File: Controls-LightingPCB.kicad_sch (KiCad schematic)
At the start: 10 parts, among them J1 PeripheralCANConnector, U1 PeripheralSOM

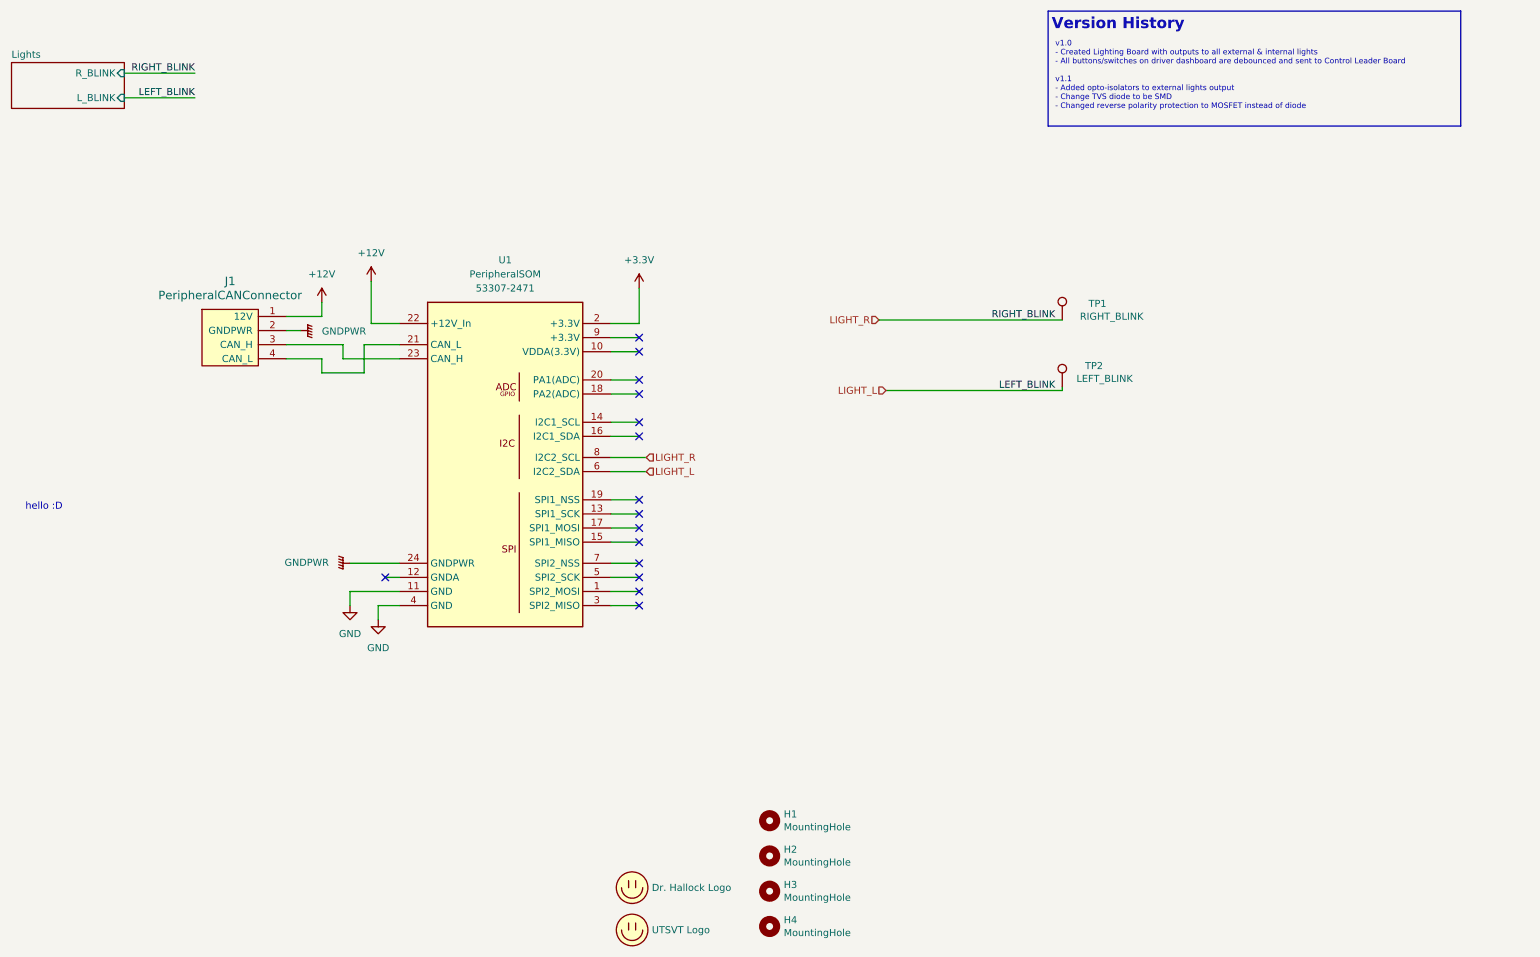
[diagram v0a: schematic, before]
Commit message: accommodated for 6 lights on one board, added test points and leds on board
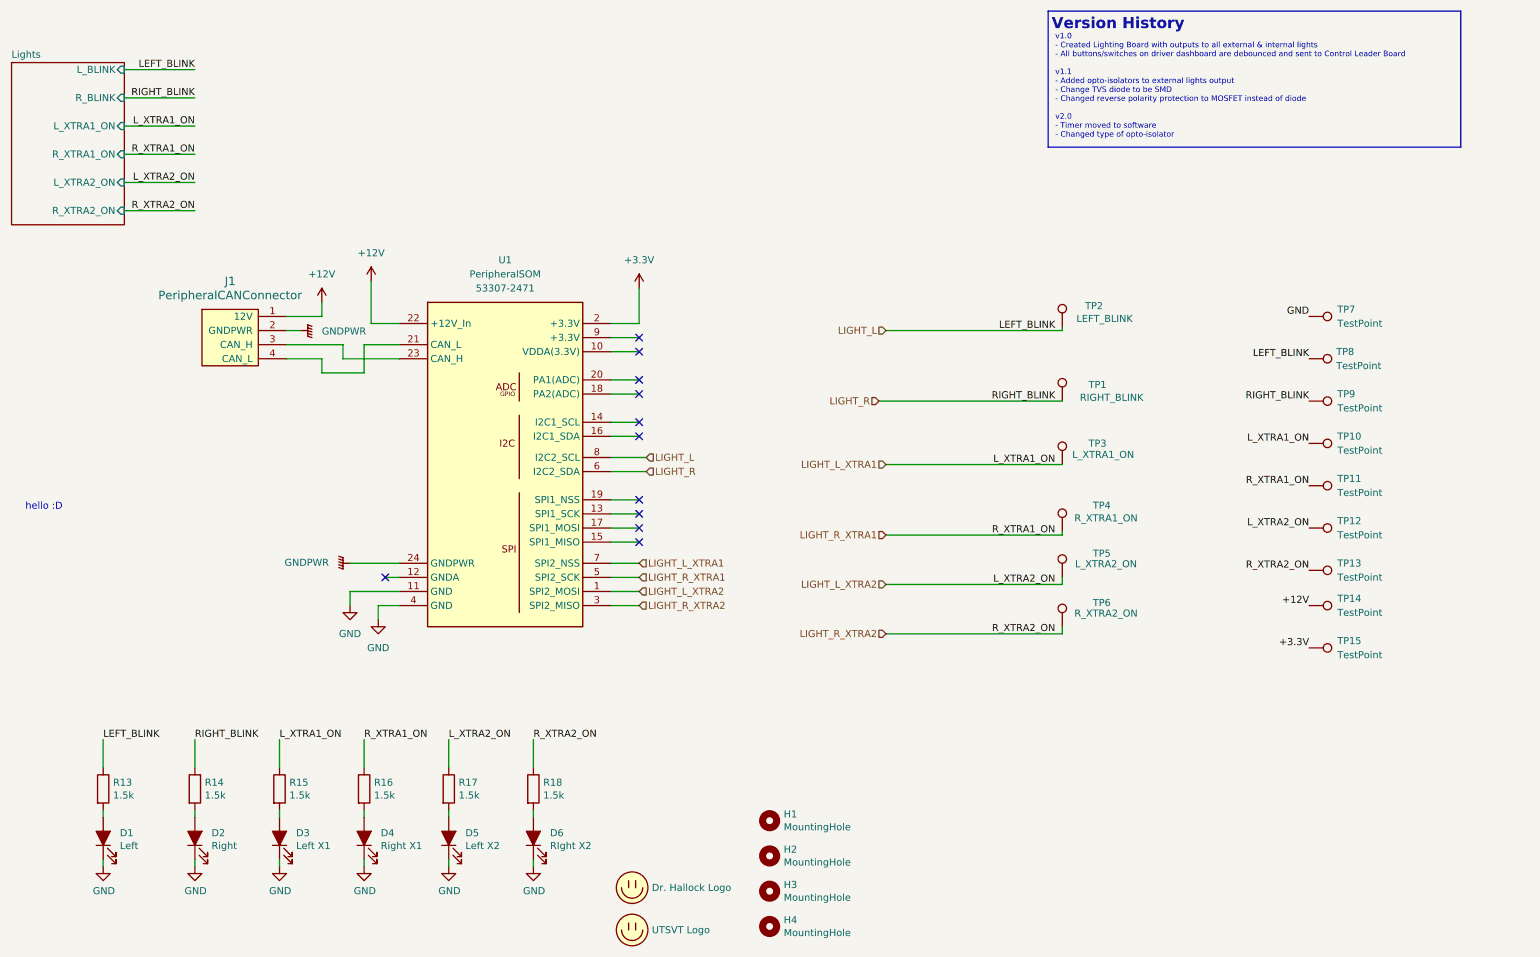
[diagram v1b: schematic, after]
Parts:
- added D1: Left, LED_SMD:LED_0805_2012Metric, symbol Device:LED_ALT
- added D2: Right, LED_SMD:LED_0805_2012Metric, symbol Device:LED_ALT
- added D3: Left X1, LED_SMD:LED_0805_2012Metric, symbol Device:LED_ALT
- added D4: Right X1, LED_SMD:LED_0805_2012Metric, symbol Device:LED_ALT
- added D5: Left X2, LED_SMD:LED_0805_2012Metric, symbol Device:LED_ALT
- added D6: RIght X2, LED_SMD:LED_0805_2012Metric, symbol Device:LED_ALT
- added R13, R14, R15, R16, R17, R18: 1.5k, Resistor_SMD:R_0805_2012Metric, symbol Device:R
- added TP10, TP11, TP12, TP13, TP14, TP15, TP7, TP8, TP9: TestPoint, symbol Connector:TestPoint
- added TP3: L_XTRA1_ON, TestPoint:TestPoint_Pad_1.5x1.5mm, symbol Connector:TestPoint
- added TP4: R_XTRA1_ON, TestPoint:TestPoint_Pad_1.5x1.5mm, symbol Connector:TestPoint
- added TP5: L_XTRA2_ON, TestPoint:TestPoint_Pad_1.5x1.5mm, symbol Connector:TestPoint
- added TP6: R_XTRA2_ON, TestPoint:TestPoint_Pad_1.5x1.5mm, symbol Connector:TestPoint
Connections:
- net +12V: now also TP14.1
- net +3.3V: now also TP15.1
- net GND: now also D1.1 (K), D2.1 (K), D3.1 (K), D4.1 (K), D5.1 (K), D6.1 (K), TP7.1
- net LIGHT_L: now also U1.8 (I2C2_SCL), R13.1, TP8.1; no longer U1.6 (I2C2_SDA)
- net LIGHT_R: now also U1.6 (I2C2_SDA), R14.1, TP9.1; no longer U1.8 (I2C2_SCL)
- net LIGHT_L_XTRA2: now reaches U1.1 (SPI2_MOSI)
- net LIGHT_L_XTRA2: now also R17.1, TP12.1, TP5.1
- net LIGHT_R_XTRA2: now reaches U1.3 (SPI2_MISO)
- net LIGHT_R_XTRA2: now also R18.1, TP13.1, TP6.1
- net LIGHT_R_XTRA1: now reaches U1.5 (SPI2_SCK)
- net LIGHT_R_XTRA1: now also R16.1, TP11.1, TP4.1
- net LIGHT_L_XTRA1: now reaches U1.7 (SPI2_NSS)
- net LIGHT_L_XTRA1: now also R15.1, TP10.1, TP3.1
- new net: D6.2 (A), R18.2
- new net: D2.2 (A), R14.2
- new net: D5.2 (A), R17.2
- new net: D4.2 (A), R16.2
- new net: D1.2 (A), R13.2
- new net: D3.2 (A), R15.2
- no-connect marks 15 -> 11
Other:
- sheet Lights ports: added L_XTRA1_ON, L_XTRA2_ON, R_XTRA1_ON, R_XTRA2_ON; removed none
- note added: "v1.0 - Created Lighting Board with outputs to all external & internal lights - All buttons/switches on driver dashboard are debounced and sent to Control Leader Board v1.1 - Added opto-isolators to external lights output - Change TVS diode to be SMD - Changed reverse polarity protection to MOSFET instead of diode v2.0 - Timer moved to software - Changed type of opto-isolator"
- note removed: "v1.0 - Created Lighting Board with outputs to all external & internal lights - All buttons/switches on driver dashboard are debounced and sent to Control Leader Board v1.1 - Added opto-isolators to external lights output - Change TVS diode to be SMD - Changed reverse polarity protection to MOSFET instead of diode"
- moved on the sheet: TP1, TP2

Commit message: simplified circuit and reduced testpoints
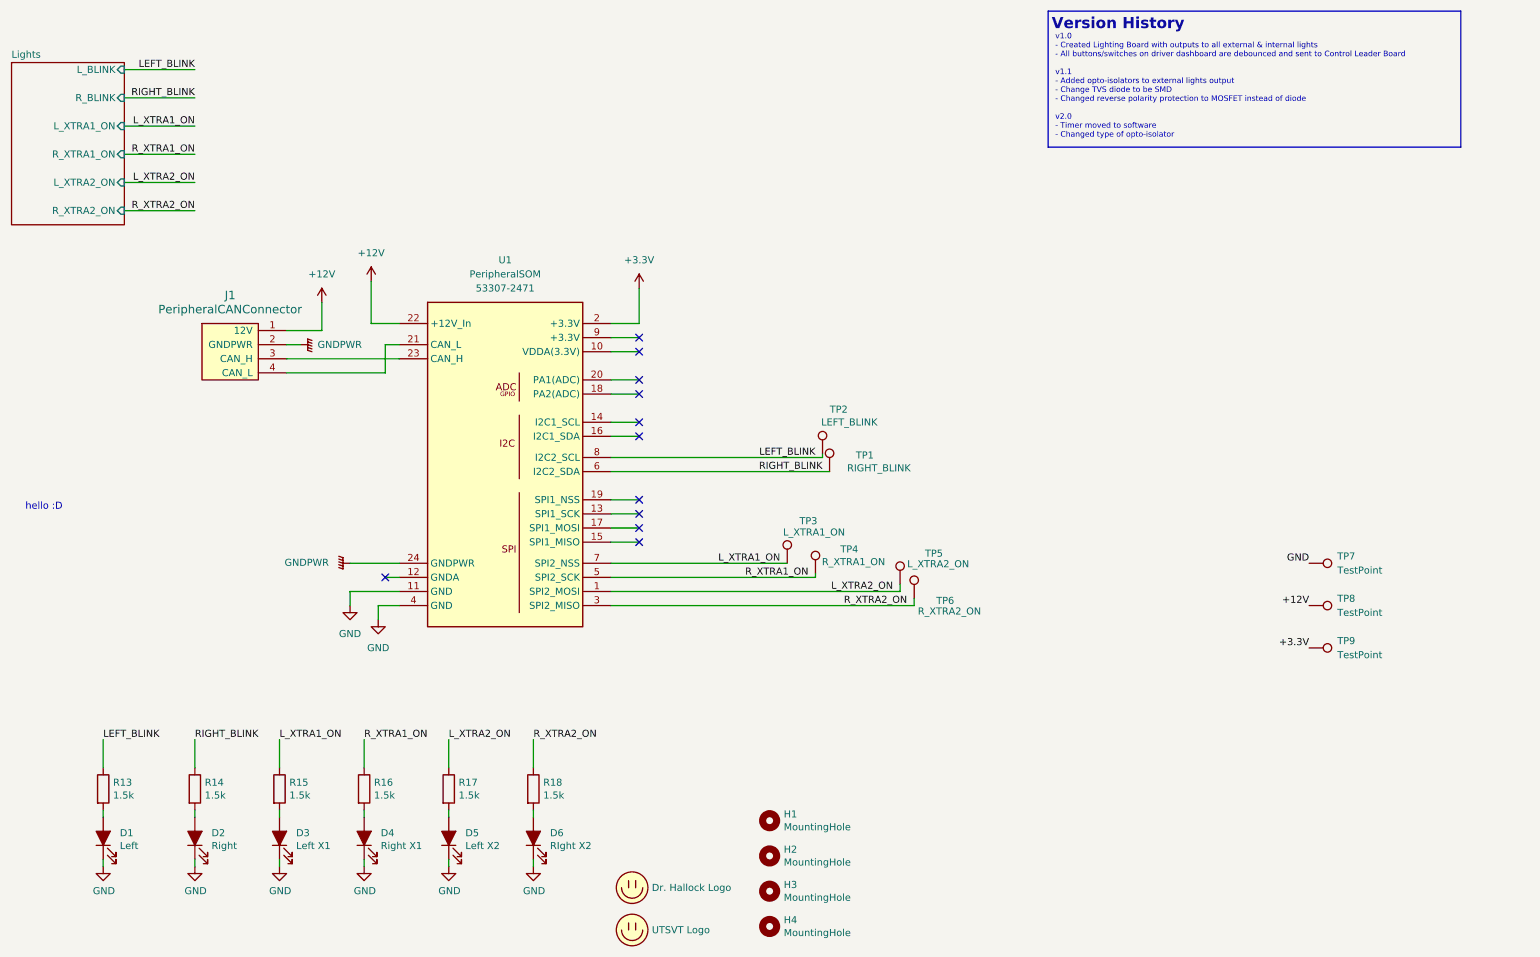
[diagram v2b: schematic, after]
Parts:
- removed TP10, TP11, TP12, TP13, TP8, TP9: TestPoint, symbol Connector:TestPoint
- renumbered TP14 to TP8, TP15 to TP9
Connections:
- net LIGHT_L renamed LEFT_BLINK
- net LIGHT_L_XTRA1 renamed L_XTRA1_ON
- net LIGHT_L_XTRA2 renamed L_XTRA2_ON
- net LIGHT_R renamed RIGHT_BLINK
- net LIGHT_R_XTRA1 renamed R_XTRA1_ON
- net LIGHT_R_XTRA2 renamed R_XTRA2_ON
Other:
- moved on the sheet: J1, TP1, TP2, TP3, TP4, TP5, TP6, TP7

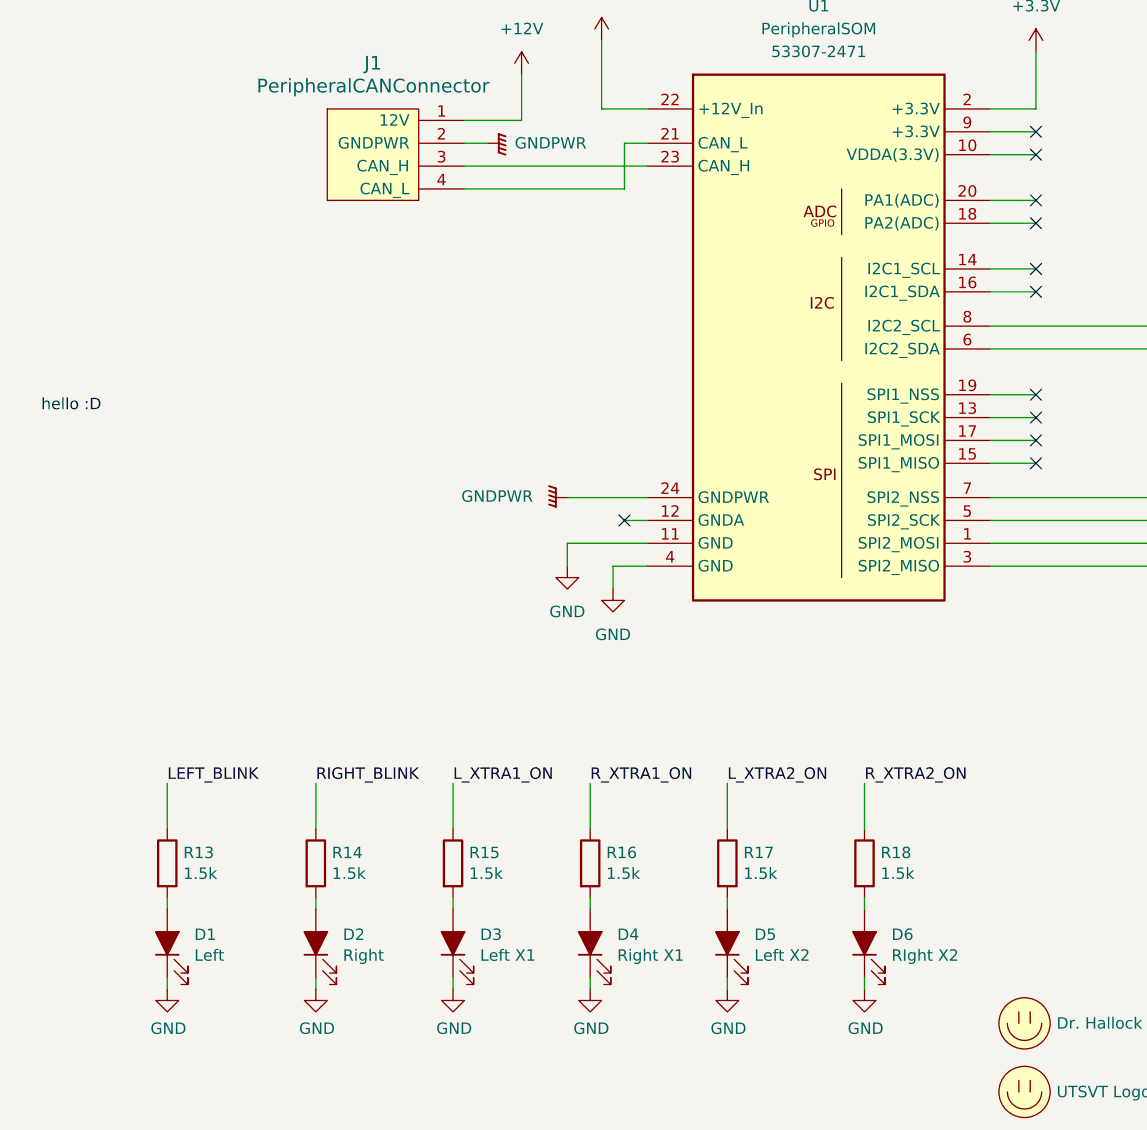
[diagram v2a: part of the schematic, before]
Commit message: added second can connector and changed resistor values for SMD LEDs
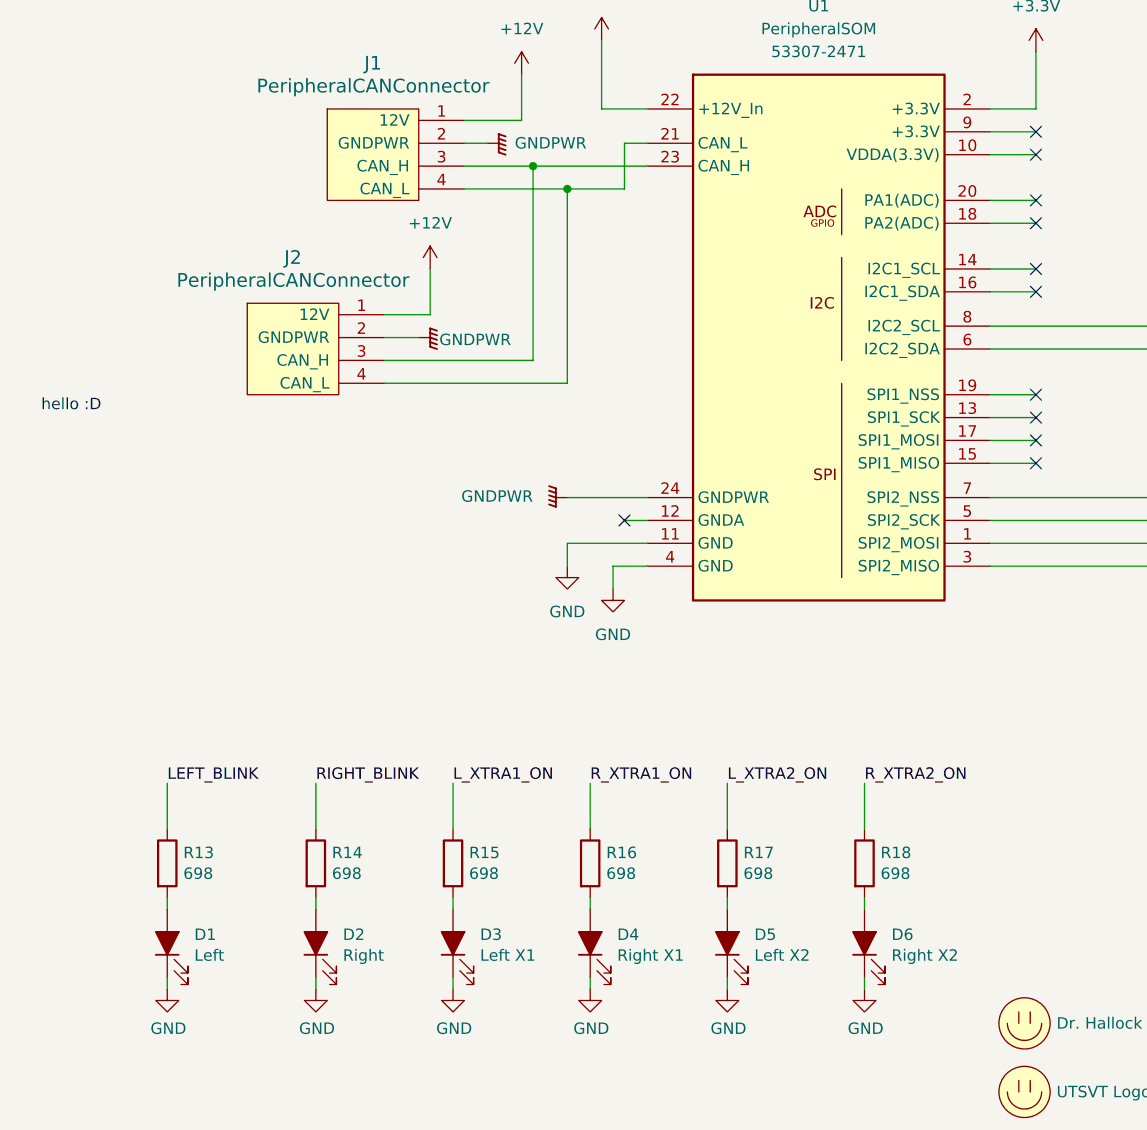
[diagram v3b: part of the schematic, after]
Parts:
- added J2: PeripheralCANConnector, UTSVT_Connectors:Molex_MicroFit3.0_1x4xP3.00mm_PolarizingPeg_Vertical, symbol utsvt-connectors:PeripheralCANConnector
- D6: value RIght X2 -> Right X2
- R13, R14, R15, R16, R17, R18: value 1.5k -> 698
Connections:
- net +12V: now also J2.1 (12V)
- net GNDPWR: now also J2.2 (GNDPWR)
- net at J1.3 (CAN_H), U1.23 (CAN_H): now also J2.3 (CAN_H)
- net at J1.4 (CAN_L), U1.21 (CAN_L): now also J2.4 (CAN_L)
